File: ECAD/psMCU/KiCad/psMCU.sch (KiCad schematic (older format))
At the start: 0 parts

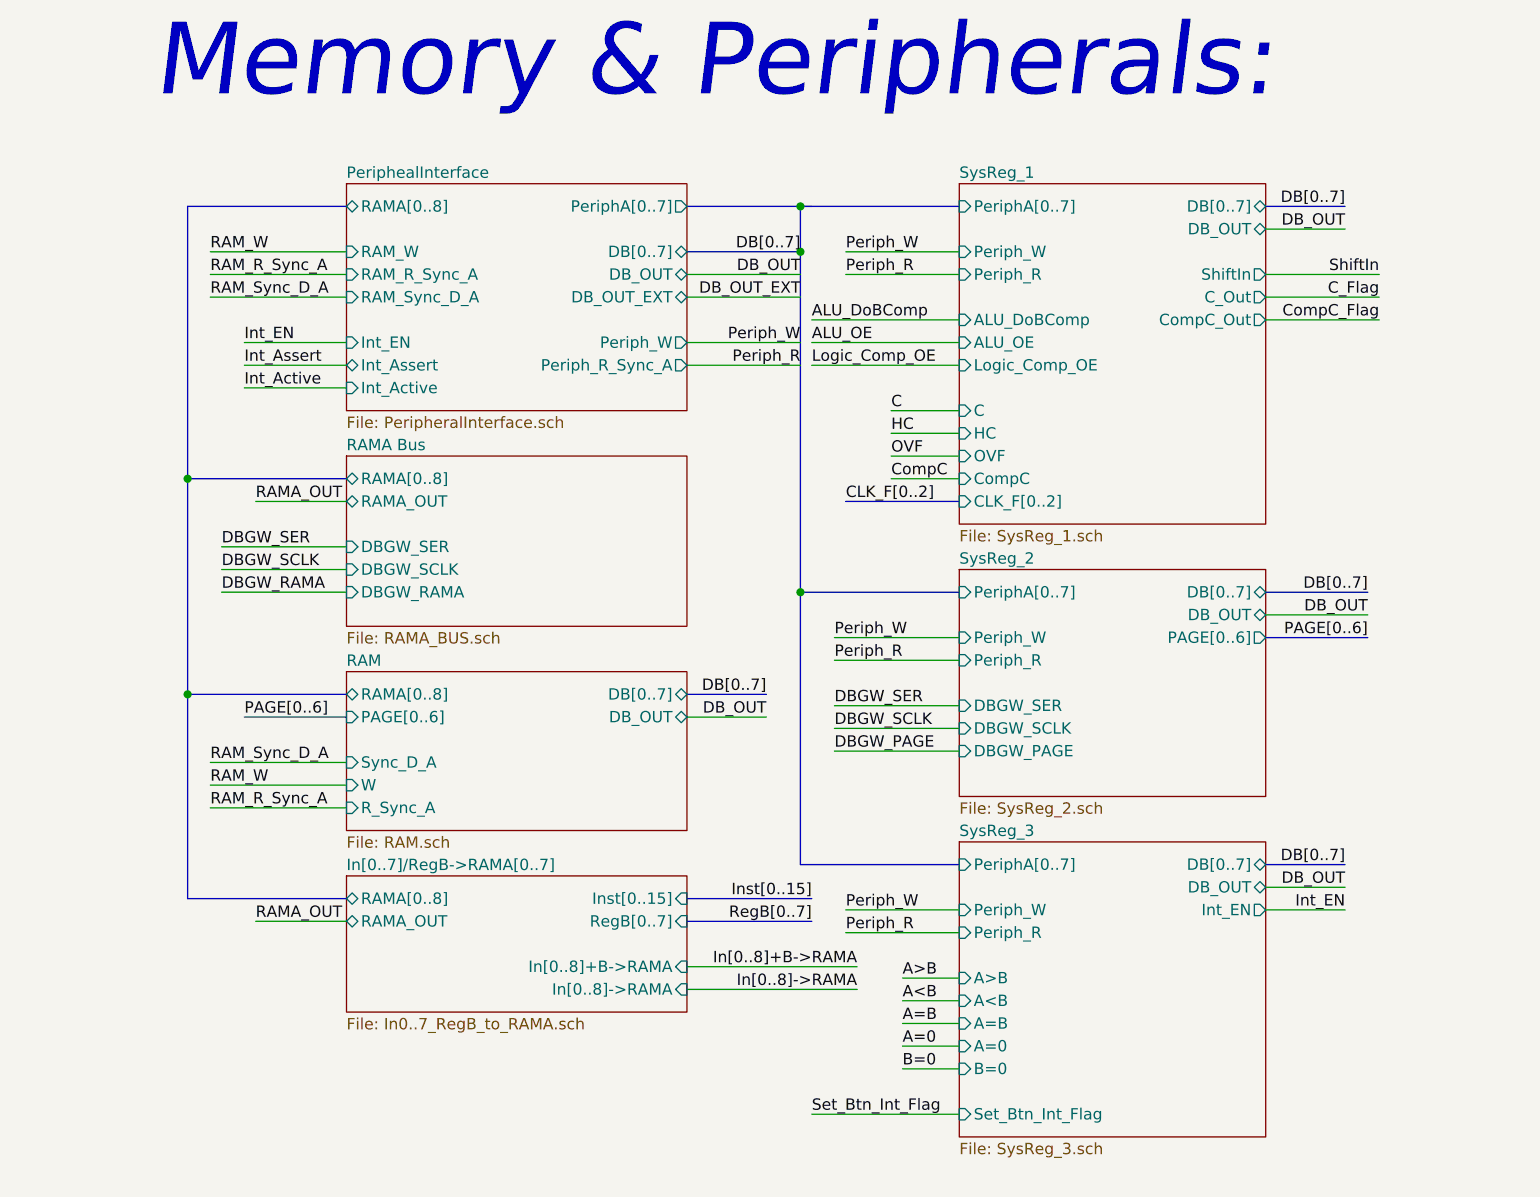
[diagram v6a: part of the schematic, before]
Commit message: Sch: Addded Buffer for external interrupt assert
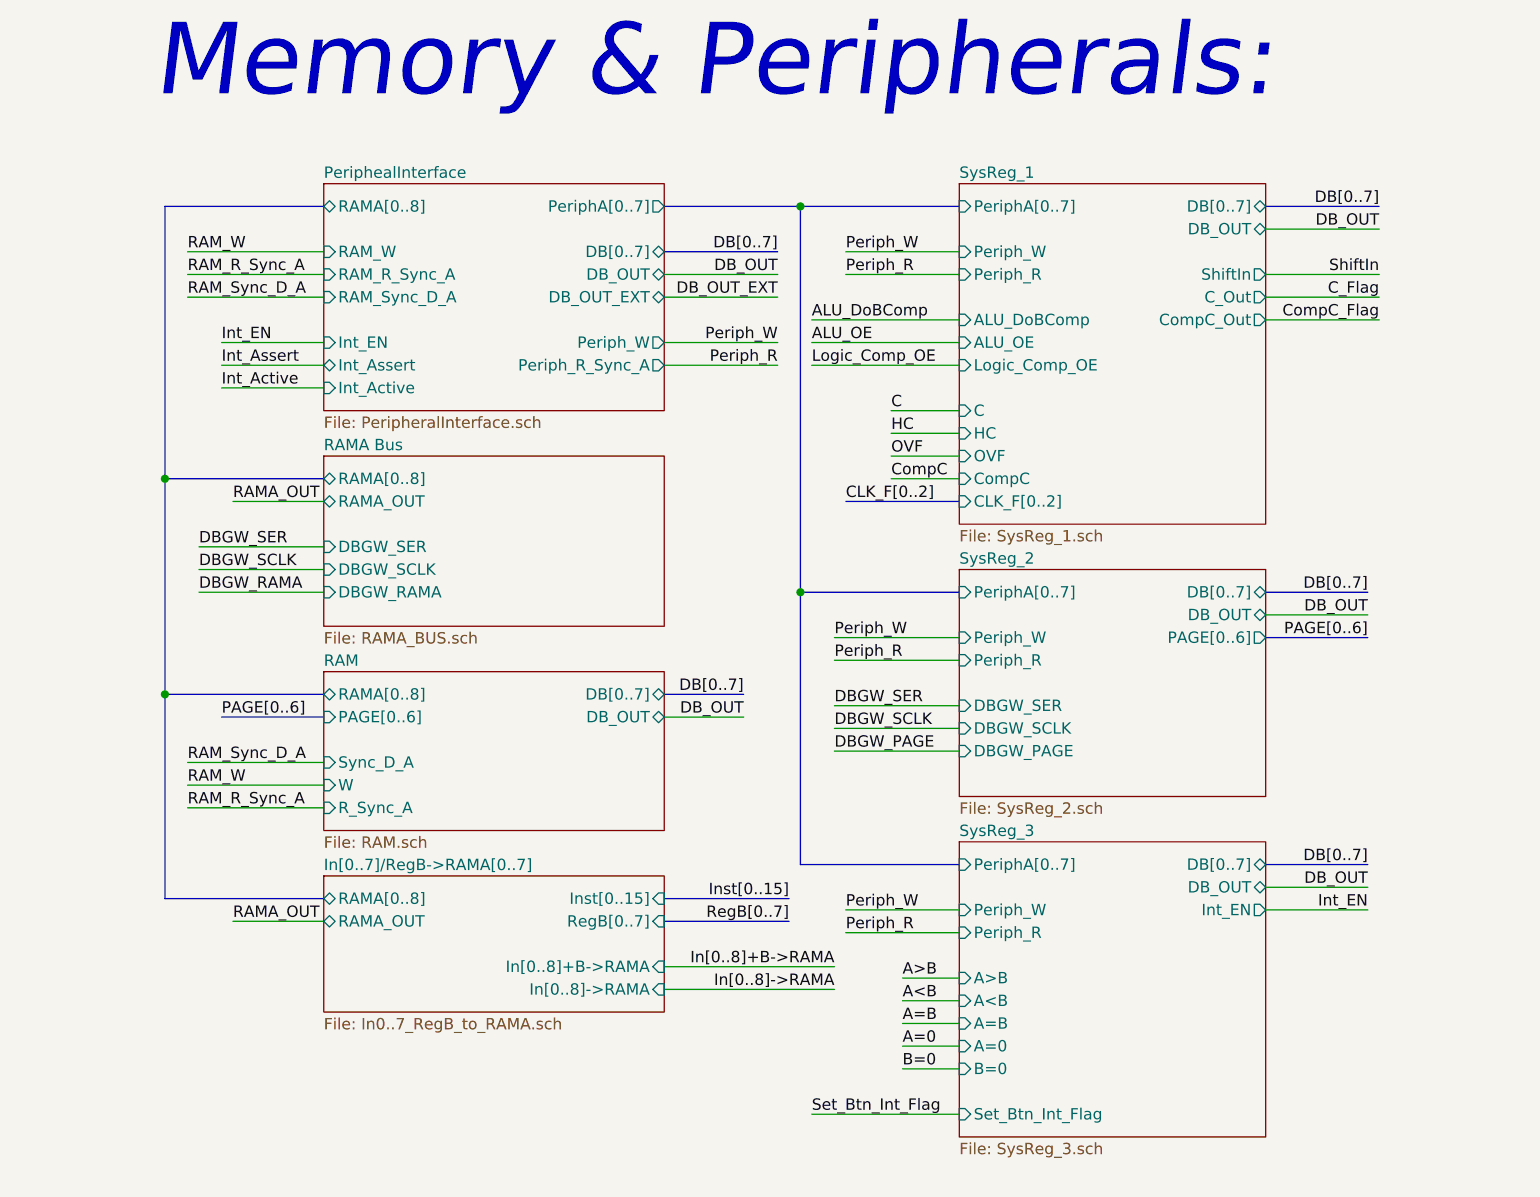
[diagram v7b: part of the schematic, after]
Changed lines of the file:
@@
 $EndSheet
 Wire Bus Line
-	3500 4600 2950 4600
-Text Label 3500 4600 2    50   ~ 0
+	3400 4600 2850 4600
+Text Label 3400 4600 2    50   ~ 0
 RegB[0..7]
 Text Notes 600  1000 0    315  Italic 0
@@
 \n
 $Sheet
-S 1450 3500 1500 700
+S 1350 3500 1500 700
 U 5ED3C49A
 F0 "RAM" 50
 F1 "RAM.sch" 50
-F2 "DB[0..7]" T R 2950 3600 50
-F3 "RAMA[0..8]" B L 1450 3600 50
-F4 "DB_OUT" T R 2950 3700 50
-F5 "PAGE[0..6]" I L 1450 3700 50
-F6 "Sync_D_A" I L 1450 3900 50
-F7 "W" I L 1450 4000 50
-F8 "R_Sync_A" I L 1450 4100 50
-$EndSheet
-$Sheet
-S 1450 4400 1500 600
+F2 "DB[0..7]" T R 2850 3600 50
+F3 "RAMA[0..8]" B L 1350 3600 50
+F4 "DB_OUT" T R 2850 3700 50
+F5 "PAGE[0..6]" I L 1350 3700 50
+F6 "Sync_D_A" I L 1350 3900 50
+F7 "W" I L 1350 4000 50
+F8 "R_Sync_A" I L 1350 4100 50
+$EndSheet
+$Sheet
+S 1350 4400 1500 600
 U 5F6FD493
 F0 "In[0..7]/RegB->RAMA[0..7]" 50
 F1 "In0..7_RegB_to_RAMA.sch" 50
-F2 "Inst[0..15]" I R 2950 4500 50
-F3 "RegB[0..7]" I R 2950 4600 50
-F4 "RAMA[0..8]" B L 1450 4500 50
-F5 "RAMA_OUT" T L 1450 4600 50
-F6 "In[0..8]+B->RAMA" I R 2950 4800 50
-F7 "In[0..8]->RAMA" I R 2950 4900 50
-$EndSheet
-Wire Bus Line
-	1450 3700 1000 3700
-Text Label 1000 3700 0    50   ~ 0
+F2 "Inst[0..15]" I R 2850 4500 50
+F3 "RegB[0..7]" I R 2850 4600 50
+F4 "RAMA[0..8]" B L 1350 4500 50
+F5 "RAMA_OUT" T L 1350 4600 50
+F6 "In[0..8]+B->RAMA" I R 2850 4800 50
+F7 "In[0..8]->RAMA" I R 2850 4900 50
+$EndSheet
+Wire Bus Line
+	1350 3700 900  3700
+Text Label 900  3700 0    50   ~ 0
 PAGE[0..6]
 Wire Wire Line
@@
 DB[0..7]
 Wire Wire Line
-	2950 3700 3300 3700
-Text Label 3300 3700 2    50   ~ 0
+	2850 3700 3200 3700
+Text Label 3200 3700 2    50   ~ 0
 DB_OUT
 Wire Bus Line
-	2950 3600 3300 3600
-Text Label 3300 3600 2    50   ~ 0
+	2850 3600 3200 3600
+Text Label 3200 3600 2    50   ~ 0
 DB[0..7]
-Text Label 1050 2750 0    50   ~ 0
+Text Label 950  2750 0    50   ~ 0
 RAMA_OUT
 Wire Wire Line
-	1050 2750 1450 2750
-Text Label 3450 1650 2    50   ~ 0
+	950  2750 1350 2750
+Text Label 3350 1650 2    50   ~ 0
 DB[0..7]
 Wire Bus Line
-	2950 1650 3450 1650
-Text Label 3450 1750 2    50   ~ 0
+	2850 1650 3350 1650
+Text Label 3350 1750 2    50   ~ 0
 DB_OUT
 Wire Wire Line
-	2950 1750 3450 1750
-Wire Wire Line
-	1450 2150 1000 2150
+	2850 1750 3350 1750
+Wire Wire Line
+	1350 2150 900  2150
 Text Label 5950 3150 2    50   ~ 0
 DB[0..7]
 Wire Bus Line
 	5500 3150 5950 3150
-Text Label 5850 1450 2    50   ~ 0
+Text Label 6000 1450 2    50   ~ 0
 DB[0..7]
 Wire Bus Line
-	5500 1450 5850 1450
+	5500 1450 6000 1450
 Wire Bus Line
 	4150 3150 3450 3150
-Wire Bus Line
-	4150 1450 3450 1450
 Text Label 5950 3350 2    50   ~ 0
 PAGE[0..6]
@@
 Wire Wire Line
 	5500 3250 5950 3250
-Text Label 5850 1550 2    50   ~ 0
+Text Label 6000 1550 2    50   ~ 0
 DB_OUT
 Wire Wire Line
-	5500 1550 5850 1550
+	5500 1550 6000 1550
 $Sheet
 S 4150 3050 1350 1000
@@
 Text Notes 3300 1350 0    50   ~ 0
 \n\n
-Text Label 1050 4600 0    50   ~ 0
+Text Label 950  4600 0    50   ~ 0
 RAMA_OUT
 Wire Wire Line
-	1050 4600 1450 4600
+	950  4600 1350 4600
 Wire Wire Line
 	5500 1750 6000 1750
 Text Label 6000 1750 2    50   ~ 0
 ShiftIn
-Text Label 1000 2150 0    50   ~ 0
+Text Label 900  2150 0    50   ~ 0
 Int_Assert
-$Sheet
-S 1450 1350 1500 1000
-U 5FD1E173
-F0 "PeriphealInterface" 50
-F1 "PeripheralInterface.sch" 50
-F2 "DB[0..7]" T R 2950 1650 50
-F3 "DB_OUT" T R 2950 1750 50
-F4 "RAMA[0..8]" B L 1450 1450 50
-F5 "RAM_Sync_D_A" I L 1450 1850 50
-F6 "RAM_W" I L 1450 1650 50
-F7 "RAM_R_Sync_A" I L 1450 1750 50
-F8 "Periph_W" O R 2950 2050 50
-F9 "PeriphA[0..7]" O R 2950 1450 50
-F10 "Int_Active" I L 1450 2250 50
-F11 "Int_Assert" B L 1450 2150 50
-F12 "Int_EN" I L 1450 2050 50
-F13 "Periph_R_Sync_A" O R 2950 2150 50
-F14 "DB_OUT_EXT" T R 2950 1850 50
-$EndSheet
-Wire Wire Line
-	1450 2250 1000 2250
-Text Label 1000 2250 0    50   ~ 0
+Wire Wire Line
+	1350 2250 900  2250
+Text Label 900  2250 0    50   ~ 0
 Int_Active
-Text Label 1000 2050 0    50   ~ 0
+Text Label 900  2050 0    50   ~ 0
 Int_EN
 Wire Wire Line
-	1000 2050 1450 2050
-Text Label 3450 2050 2    50   ~ 0
+	900  2050 1350 2050
+Text Label 3350 2050 2    50   ~ 0
 Periph_W
-Text Label 3450 2150 2    50   ~ 0
+Text Label 3350 2150 2    50   ~ 0
 Periph_R
 Wire Wire Line
-	3450 2050 2950 2050
-Wire Wire Line
-	2950 2150 3450 2150
+	3350 2050 2850 2050
+Wire Wire Line
+	2850 2150 3350 2150
 Text Label 3650 1650 0    50   ~ 0
 Periph_W
@@
 C
 Wire Wire Line
-	1450 1650 850  1650
-Text Label 850  1650 0    50   ~ 0
+	1350 1650 750  1650
+Text Label 750  1650 0    50   ~ 0
 RAM_W
-Text Label 850  1750 0    50   ~ 0
+Text Label 750  1750 0    50   ~ 0
 RAM_R_Sync_A
-Text Label 850  1850 0    50   ~ 0
+Text Label 750  1850 0    50   ~ 0
 RAM_Sync_D_A
 Wire Wire Line
-	850  1750 1450 1750
-Wire Wire Line
-	850  1850 1450 1850
+	750  1750 1350 1750
+Wire Wire Line
+	750  1850 1350 1850
 Text Label 3650 2750 0    50   ~ 0
 CLK_F[0..2]
@@
 $EndSheet
 Wire Wire Line
-	5500 4550 5850 4550
-Text Label 5850 4550 2    50   ~ 0
+	5500 4550 5950 4550
+Text Label 5950 4550 2    50   ~ 0
 Int_EN
 Wire Wire Line
-	5500 4450 5850 4450
-Text Label 5850 4450 2    50   ~ 0
+	5500 4450 5950 4450
+Text Label 5950 4450 2    50   ~ 0
 DB_OUT
 Wire Bus Line
 	3450 4350 4150 4350
 Wire Bus Line
-	5500 4350 5850 4350
-Text Label 5850 4350 2    50   ~ 0
+	5500 4350 5950 4350
+Text Label 5950 4350 2    50   ~ 0
 DB[0..7]
 Text Label 3500 5450 0    50   ~ 0
@@
 	3500 5450 4150 5450
 Wire Bus Line
-	2950 4500 3500 4500
-Text Label 3500 4500 2    50   ~ 0
+	2850 4500 3400 4500
+Text Label 3400 4500 2    50   ~ 0
 Inst[0..15]
 Wire Bus Line
-	750  2650 1450 2650
+	650  2650 1350 2650
 Text Notes 5000 -3300 0    79   ~ 0
  - 8bit Processor\n - 1MHz Clock\n - 32kB Heap RAM, \n - 32kB Stack RAM\n - 16kB Program ROM\n
@@
 Cond
 Wire Wire Line
-	850  3900 1450 3900
-Wire Wire Line
-	850  4100 1450 4100
-Text Label 850  3900 0    50   ~ 0
+	750  3900 1350 3900
+Wire Wire Line
+	750  4100 1350 4100
+Text Label 750  3900 0    50   ~ 0
 RAM_Sync_D_A
-Text Label 850  4100 0    50   ~ 0
+Text Label 750  4100 0    50   ~ 0
 RAM_R_Sync_A
-Text Label 850  4000 0    50   ~ 0
+Text Label 750  4000 0    50   ~ 0
 RAM_W
 Wire Wire Line
-	1450 4000 850  4000
-Wire Bus Line
-	1450 1450 750  1450
-Wire Bus Line
-	1450 3600 750  3600
+	1350 4000 750  4000
+Wire Bus Line
+	1350 1450 650  1450
+Wire Bus Line
+	1350 3600 650  3600
 Text Label -3300 1800 0    50   ~ 0
 Inst[0..15]
@@
 Wire Bus Line
 	9950 2900 10650 2900
-Wire Bus Line
-	2950 1450 3450 1450
 Connection ~ 5400 9000
 Wire Bus Line
@@
 Wire Bus Line
 	3200 7150 3200 7450
-Text Label 3700 4800 2    50   ~ 0
+Text Label 3600 4800 2    50   ~ 0
 In[0..8]+B->RAMA
-Text Label 3700 4900 2    50   ~ 0
+Text Label 3600 4900 2    50   ~ 0
 In[0..8]->RAMA
 Wire Wire Line
-	2950 4800 3700 4800
-Wire Wire Line
-	2950 4900 3700 4900
+	2850 4800 3600 4800
+Wire Wire Line
+	2850 4900 3600 4900
 Wire Bus Line
 	11850 2900 12200 2900
@@
 	14750 3900 15600 3900
 Wire Wire Line
-	3450 1850 2950 1850
-Text Label 3450 1850 2    50   ~ 0
+	3350 1850 2850 1850
+Text Label 3350 1850 2    50   ~ 0
 DB_OUT_EXT
 Text Label 3300 9700 0    50   ~ 0
@@
 Connection ~ 3450 3150
 Wire Bus Line
-	750  4500 1450 4500
+	650  4500 1350 4500
 Wire Bus Line
 	9950 2500 10650 2500
@@
 $EndSheet
 $Sheet
-S 1450 2550 1500 750
+S 1350 2550 1500 750
 U 604F08FB
 F0 "RAMA Bus" 50
 F1 "RAMA_BUS.sch" 50
-F2 "RAMA[0..8]" T L 1450 2650 50
-F3 "RAMA_OUT" T L 1450 2750 50
-F4 "DBGW_RAMA" I L 1450 3150 50
-F5 "DBGW_SER" I L 1450 2950 50
-F6 "DBGW_SCLK" I L 1450 3050 50
+F2 "RAMA[0..8]" T L 1350 2650 50
+F3 "RAMA_OUT" T L 1350 2750 50
+F4 "DBGW_RAMA" I L 1350 3150 50
+F5 "DBGW_SER" I L 1350 2950 50
+F6 "DBGW_SCLK" I L 1350 3050 50
 $EndSheet
 $Sheet
@@
 DBGW_STCK
 Wire Bus Line
-	750  3600 750  2650
-Connection ~ 750  3600
+	650  3600 650  2650
+Connection ~ 650  3600
 Wire Wire Line
 	14700 8800 15250 8800
@@
 DBGW_RAMA
 Wire Wire Line
-	1450 3150 900  3150
-Text Label 900  3150 0    50   ~ 0
+	1350 3150 800  3150
+Text Label 800  3150 0    50   ~ 0
 DBGW_RAMA
-Text Label 900  3050 0    50   ~ 0
+Text Label 800  3050 0    50   ~ 0
 DBGW_SCLK
 Wire Wire Line
-	900  3050 1450 3050
-Wire Wire Line
-	1450 2950 900  2950
-Text Label 900  2950 0    50   ~ 0
+	800  3050 1350 3050
+Wire Wire Line
+	1350 2950 800  2950
+Text Label 800  2950 0    50   ~ 0
 DBGW_SER
 Wire Wire Line
@@
 DBGW_SER
 Wire Bus Line
-	750  3600 750  4500
-Connection ~ 3450 1450
-Wire Bus Line
-	3450 1450 3450 1650
-Connection ~ 3450 1650
-Wire Bus Line
-	3450 1650 3450 3150
-Wire Bus Line
-	3450 1450 3500 1450
-Wire Bus Line
-	750  2650 750  1450
-Connection ~ 750  2650
+	650  3600 650  4500
+Wire Bus Line
+	650  2650 650  1450
+Connection ~ 650  2650
 Wire Wire Line
 	14700 9250 15250 9250
@@
 Wire Wire Line
 	8550 8900 9050 8900
+Wire Bus Line
+	3450 1450 3450 3150
+Wire Bus Line
+	2850 1450 3450 1450
+Connection ~ 3450 1450
+Wire Bus Line
+	3450 1450 4150 1450
+$Sheet
+S 1350 1350 1500 1000
+U 5FD1E173
+F0 "PeriphealInterface" 50
+F1 "PeripheralInterface.sch" 50
+F2 "DB[0..7]" T R 2850 1650 50
+F3 "DB_OUT" T R 2850 1750 50
+F4 "RAMA[0..8]" B L 1350 1450 50
+F5 "RAM_Sync_D_A" I L 1350 1850 50
+F6 "RAM_W" I L 1350 1650 50
+F7 "RAM_R_Sync_A" I L 1350 1750 50
+F8 "Periph_W" O R 2850 2050 50
+F9 "PeriphA[0..7]" O R 2850 1450 50
+F10 "Int_Active" I L 1350 2250 50
+F11 "Int_Assert" B L 1350 2150 50
+F12 "Int_EN" I L 1350 2050 50
+F13 "Periph_R_Sync_A" O R 2850 2150 50
+F14 "DB_OUT_EXT" T R 2850 1850 50
+$EndSheet
 $EndSCHEMATC

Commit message: Sch: Modified instruction set to add fast memory access functions.
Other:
- note removed: "- 300+ LEDs\n - Interrupts\n - Instruction Stepping\n - Clock Stepping\n - 1Hz-1MHz Clock\n - External remote control\n - External USB programmer\n - Hardware Call/Return\n - Peripheral Ports\n - Hardware breakpoint"
- note removed: "- 8bit Processor\n - 1MHz Clock\n - 32kB Heap RAM, \n - 32kB Stack RAM\n - 16kB Program ROM\n"
- note removed: "Features:\n"
- note removed: "Specs:"
